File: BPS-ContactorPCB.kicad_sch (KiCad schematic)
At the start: 20 parts, among them J1 BPS_PWR, J2 BPS_IN, J3 DRV_ESTOP, J4 EXT_ESTOP, J5 HV+ Contactor, J6 HV- Contactor, Q1 PMOS, Q2 PMOS, U1 SFH617A-1

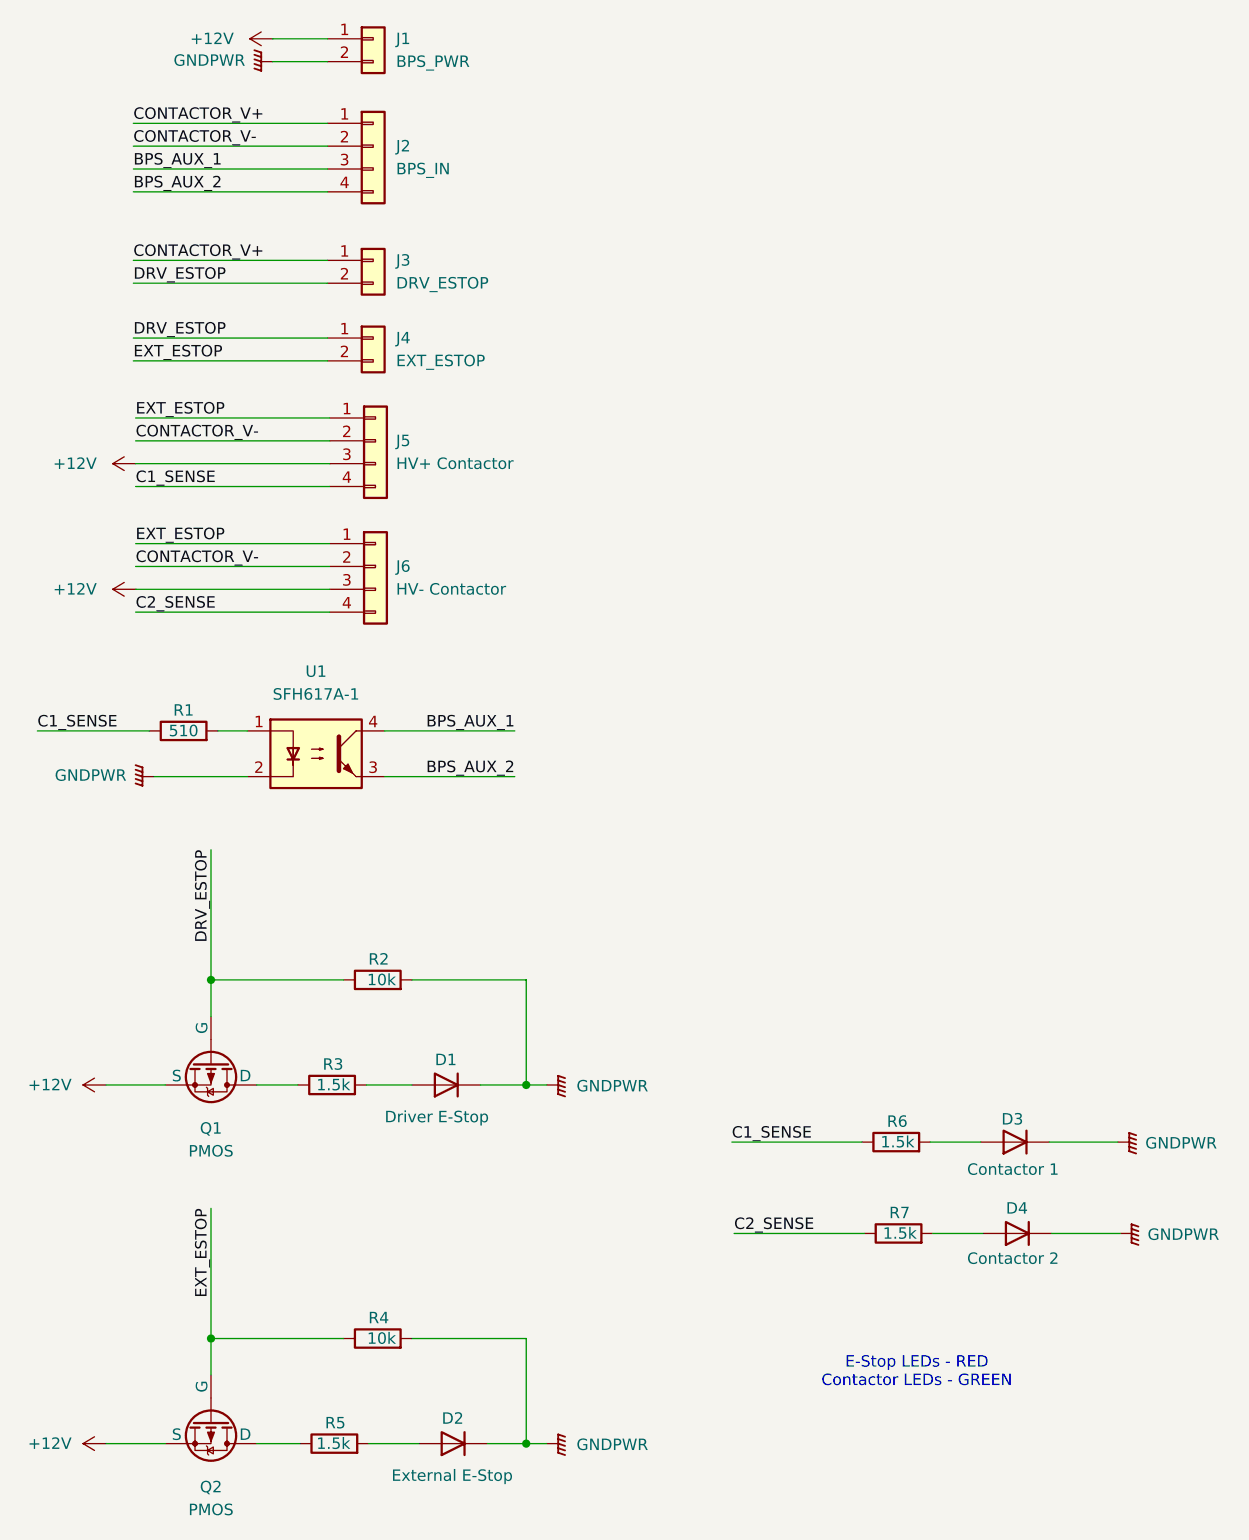
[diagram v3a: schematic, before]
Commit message: Added green status LEDs for successful contactor close
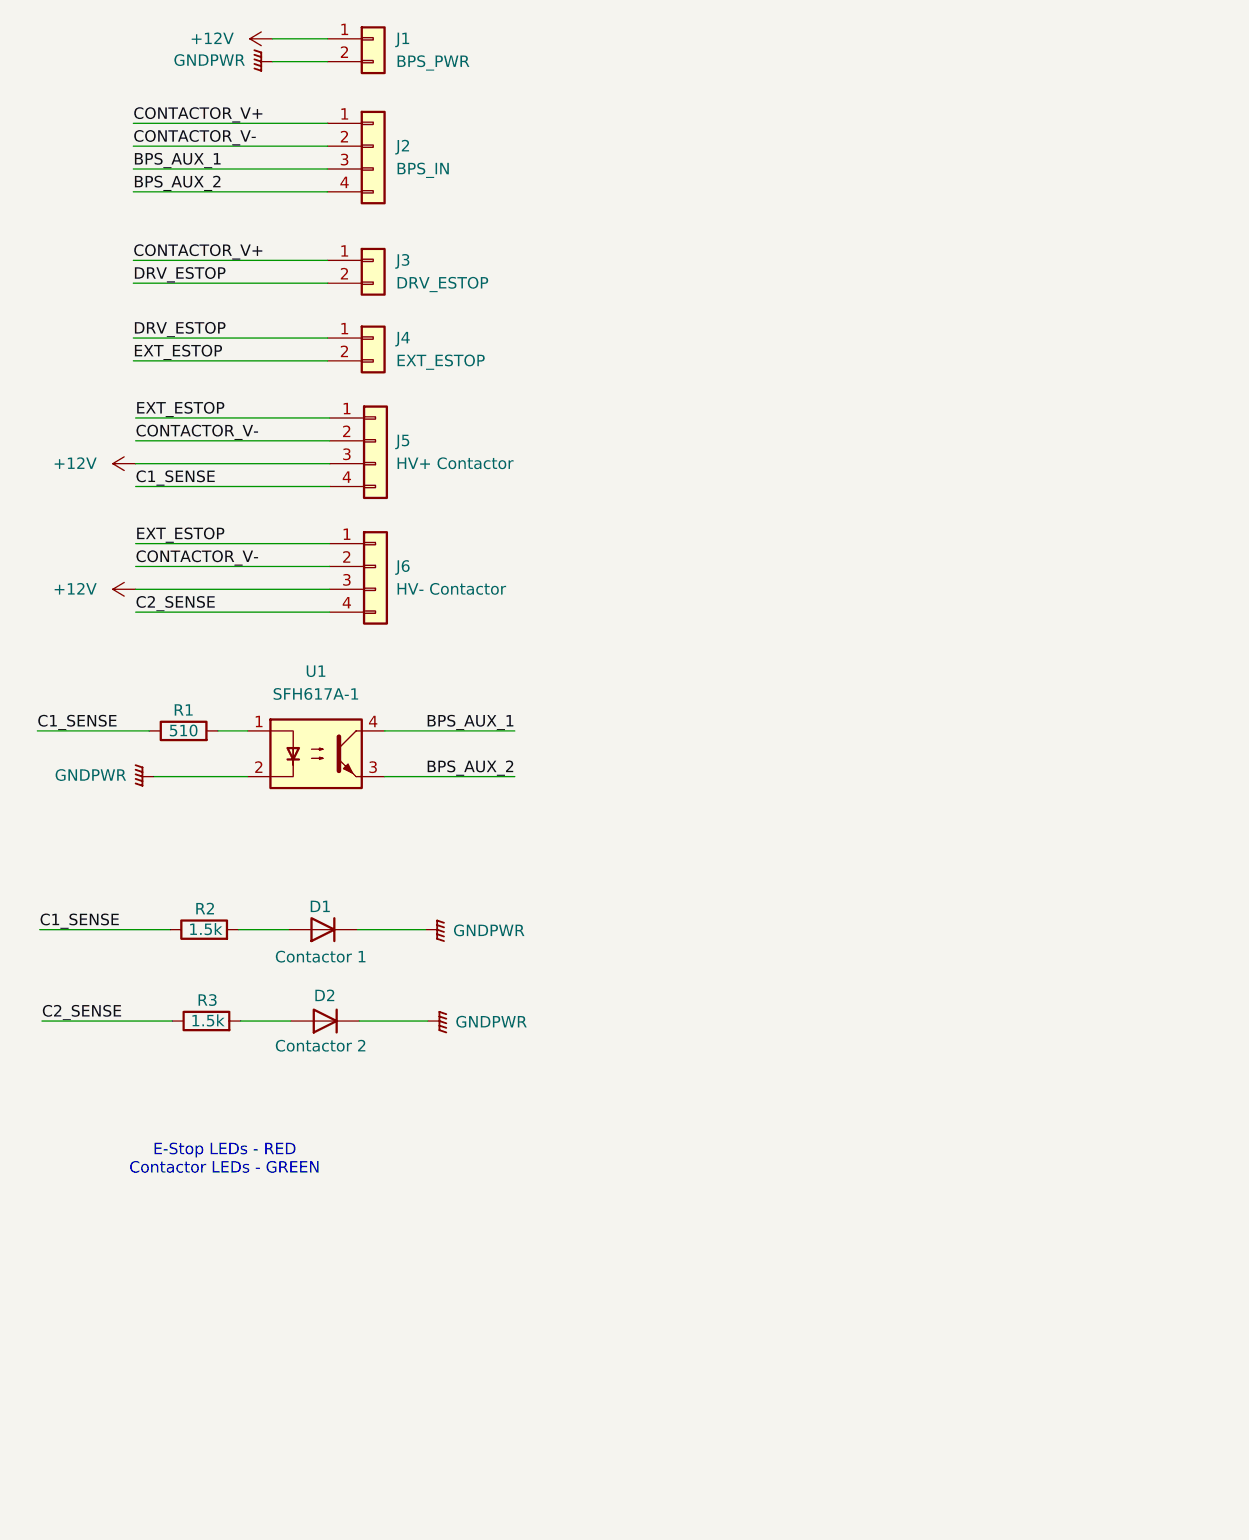
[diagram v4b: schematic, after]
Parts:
- removed D1: Driver E-Stop, LED_SMD:LED_0805_2012Metric, symbol Device:D
- removed D2: External E-Stop, LED_SMD:LED_0805_2012Metric, symbol Device:D
- removed Q1, Q2: PMOS, symbol Simulation_SPICE:PMOS
- removed R2, R4: 10k, Resistor_SMD:R_0805_2012Metric, symbol Device:R
- removed R3, R5: 1.5k, Resistor_SMD:R_0805_2012Metric, symbol Device:R
- renumbered D3 to D1, D4 to D2, R6 to R2, R7 to R3
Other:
- moved on the sheet: D1, D2, R2, R3
